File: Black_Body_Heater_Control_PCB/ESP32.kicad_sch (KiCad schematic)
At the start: 18 parts, among them J3 USB_C_Receptacle_USB2.0_14P, J4 Conn_01x04_Pin, SW1 430471035826, SW2 430471035826, U1 ESP32-S3-WROOM-1-N8R8, U4 USBLC6-2SC6, U5 MAX31865xAP

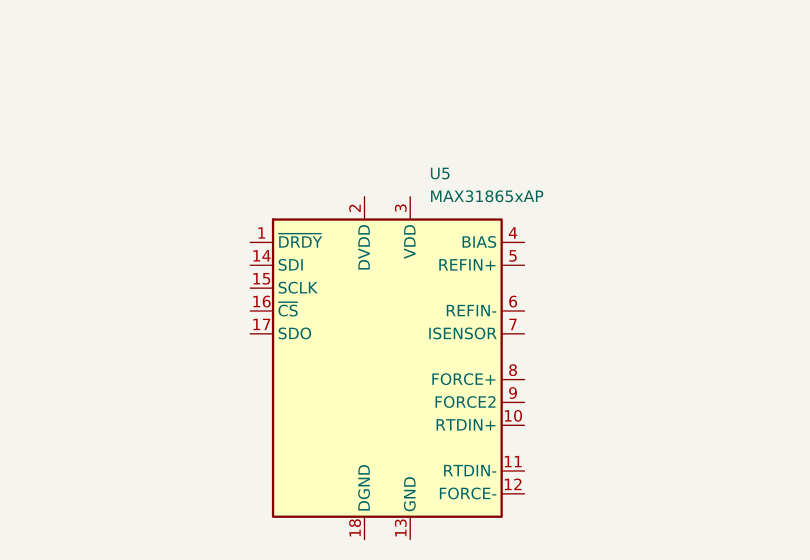
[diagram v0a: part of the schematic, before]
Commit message: Buck spice file not working, created new pcb
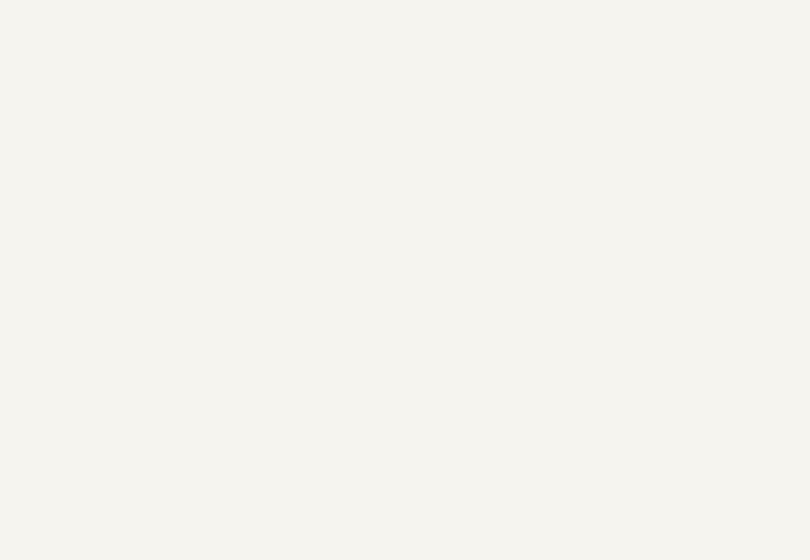
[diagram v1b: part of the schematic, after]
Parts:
- removed U5: MAX31865xAP, Package_SO:SSOP-20_5.3x7.2mm_P0.65mm, symbol Sensor_Temperature:MAX31865xAP
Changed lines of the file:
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@@
-	)
-	(symbol
-		(lib_id "Sensor_Temperature:MAX31865xAP")
-		(at 73.66 161.29 0)
-		(unit 1)
-		(body_style 1)
-		(exclude_from_sim no)
-		(in_bom yes)
-		(on_board yes)
-		(in_pos_files yes)
-		(dnp no)
-		(fields_autoplaced yes)
-		(property "Reference" "U5"
-			(at 78.3433 138.43 0)
-			(show_name no)
-			(do_not_autoplace no)
-			(effects
-				(font
-					(size 1.27 1.27)
-				)
-				(justify left)
-			)
-		)
-		(property "Value" "MAX31865xAP"
-			(at 78.3433 140.97 0)
-			(show_name no)
-			(do_not_autoplace no)
-			(effects
-				(font
-					(size 1.27 1.27)
-				)
-				(justify left)
-			)
-		)
-		(property "Footprint" "Package_SO:SSOP-20_5.3x7.2mm_P0.65mm"
-			(at 77.47 177.8 0)
-			(hide yes)
-			(show_name no)
-			(do_not_autoplace no)
-			(effects
-				(font
-					(size 1.27 1.27)
-				)
-				(justify left)
-			)
-		)
-		(property "Datasheet" "https://www.analog.com/media/en/technical-documentation/data-sheets/MAX31865.pdf"
-			(at 73.66 158.75 0)
-			(hide yes)
-			(show_name no)
-			(do_not_autoplace no)
-			(effects
-				(font
-					(size 1.27 1.27)
-				)
-			)
-		)
-		(property "Description" "RTD-to-Digital Converter, SSOP-20"
-			(at 73.66 161.29 0)
-			(hide yes)
-			(show_name no)
-			(do_not_autoplace no)
-			(effects
-				(font
-					(size 1.27 1.27)
-				)
-			)
-		)
-		(pin "2"
-		)
-		(pin "1"
-		)
-		(pin "9"
-		)
-		(pin "11"
-		)
-		(pin "7"
-		)
-		(pin "16"
-		)
-		(pin "3"
-		)
-		(pin "5"
-		)
-		(pin "8"
-		)
-		(pin "10"
-		)
-		(pin "12"
-		)
-		(pin "6"
-		)
-		(pin "13"
-		)
-		(pin "19"
-		)
-		(pin "18"
-		)
-		(pin "20"
-		)
-		(pin "17"
-		)
-		(pin "4"
-		)
-		(pin "14"
-		)
-		(pin "15"
-		)
-		(instances
-			(project "Black_Body_Heater_Control"
-				(path "/f3dd8e24-b1a1-45ed-a541-b7ae36b7e8e0/81e90e05-0519-429e-85ab-ffede3727917"
-					(reference "U5")
-					(unit 1)
-				)
-			)
-		)
 	)
 	(symbol
